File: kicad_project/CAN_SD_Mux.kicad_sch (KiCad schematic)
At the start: 2 parts, among them U13 ADG733BRU

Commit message: ERC passing!
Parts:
- removed unit 5 of U13
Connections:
- net +3.3V: now also U13.1; no longer U13.2
- net CAN_BUS: now also U13.12; no longer U13.13
- net GPOUT2: now also U13.13; no longer U13.12
- net SPI.CAN_SD_CS: now also U13.2; no longer U13.1
- net ~SD_CARD_ENABLE renamed SD_CARD_ENABLE

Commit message: Cleanups and more documentation
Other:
- moved on the sheet: C32, U13D
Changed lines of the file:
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@@
 	(generator "eeschema")
 	(generator_version "8.0")
-	(paper "A4")
+	(paper "A5")
+	(title_block
+		(comment 1 "Mux for selecting CAN signals.")
+	)
 	(junction
-		(at 57.15 172.72)
+		(at 137.16 86.36)
 		(diameter 0)
 		(color 0 0 0 0)
@@
 	)
 	(junction
-		(at 38.1 143.51)
+		(at 118.11 57.15)
 		(diameter 0)
 		(color 0 0 0 0)
 	)
 	(junction
-		(at 38.1 172.72)
+		(at 118.11 86.36)
 		(diameter 0)
 		(color 0 0 0 0)
@@
 	)
 	(junction
-		(at 44.45 172.72)
+		(at 124.46 86.36)
 		(diameter 0)
 		(color 0 0 0 0)
@@
 	(wire
 		(pts
-			(xy 35.56 142.24) (xy 35.56 143.51)
+			(xy 115.57 55.88) (xy 115.57 57.15)
 		)
 		(stroke
@@
 	(wire
 		(pts
-			(xy 38.1 143.51) (xy 57.15 143.51)
+			(xy 118.11 57.15) (xy 137.16 57.15)
 		)
 		(stroke
@@
 	(wire
 		(pts
-			(xy 44.45 172.72) (xy 38.1 172.72)
+			(xy 124.46 86.36) (xy 118.11 86.36)
 		)
 		(stroke
@@
 	(wire
 		(pts
-			(xy 44.45 158.75) (xy 44.45 172.72)
+			(xy 124.46 72.39) (xy 124.46 86.36)
 		)
 		(stroke
@@
 	(wire
 		(pts
-			(xy 35.56 143.51) (xy 38.1 143.51)
+			(xy 115.57 57.15) (xy 118.11 57.15)
 		)
 		(stroke
@@
 	(wire
 		(pts
-			(xy 57.15 143.51) (xy 57.15 146.05)
+			(xy 137.16 57.15) (xy 137.16 59.69)
 		)
 		(stroke
@@
 	(wire
 		(pts
-			(xy 49.53 158.75) (xy 44.45 158.75)
+			(xy 129.54 72.39) (xy 124.46 72.39)
 		)
 		(stroke
@@
 	(wire
 		(pts
-			(xy 38.1 172.72) (xy 35.56 172.72)
-		)
-		(stroke
-			(width 0)
-			(type default)
-		)
-	)
-	(wire
-		(pts
-			(xy 59.69 171.45) (xy 59.69 172.72)
+			(xy 118.11 86.36) (xy 115.57 86.36)
+		)
+		(stroke
+			(width 0)
+			(type default)
+		)
+	)
+	(wire
+		(pts
+			(xy 139.7 85.09) (xy 139.7 86.36)
 		)
 		(stroke
@@
 	(wire
 		(pts
-			(xy 38.1 153.67) (xy 38.1 172.72)
-		)
-		(stroke
-			(width 0)
-			(type default)
-		)
-	)
-	(wire
-		(pts
-			(xy 35.56 172.72) (xy 35.56 173.99)
+			(xy 118.11 67.31) (xy 118.11 86.36)
+		)
+		(stroke
+			(width 0)
+			(type default)
+		)
+	)
+	(wire
+		(pts
+			(xy 115.57 86.36) (xy 115.57 87.63)
 		)
 		(stroke
@@
 	(wire
 		(pts
-			(xy 59.69 172.72) (xy 57.15 172.72)
+			(xy 139.7 86.36) (xy 137.16 86.36)
 		)
 		(stroke
@@
 	(wire
 		(pts
-			(xy 57.15 172.72) (xy 44.45 172.72)
-		)
-		(stroke
-			(width 0)
-			(type default)
-		)
-	)
-	(wire
-		(pts
-			(xy 38.1 143.51) (xy 38.1 148.59)
+			(xy 137.16 86.36) (xy 124.46 86.36)
+		)
+		(stroke
+			(width 0)
+			(type default)
+		)
+	)
+	(wire
+		(pts
+			(xy 118.11 57.15) (xy 118.11 62.23)
 		)
 		(stroke
@@
 	(wire
 		(pts
-			(xy 57.15 171.45) (xy 57.15 172.72)
+			(xy 137.16 85.09) (xy 137.16 86.36)
 		)
 		(stroke
@@
 	(symbol
 		(lib_id "power:GND")
-		(at 35.56 173.99 0)
+		(at 115.57 87.63 0)
 		(unit 1)
 		(exclude_from_sim no)
@@
 		(fields_autoplaced yes)
 		(property "Reference" "#PWR0105"
-			(at 35.56 180.34 0)
+			(at 115.57 93.98 0)
 			(effects
 				(font
@@
 		)
 		(property "Value" "GND"
-			(at 35.56 179.07 0)
+			(at 115.57 92.71 0)
 			(effects
 				(font
@@
 		)
 		(property "Footprint" ""
-			(at 35.56 173.99 0)
+			(at 115.57 87.63 0)
 			(effects
 				(font
@@
 		)
 		(property "Datasheet" ""
-			(at 35.56 173.99 0)
+			(at 115.57 87.63 0)
 			(effects
 				(font
@@
 		)
 		(property "Description" "Power symbol creates a global label with name \"GND\" , ground"
-			(at 35.56 173.99 0)
+			(at 115.57 87.63 0)
 			(effects
 				(font
@@
 	(symbol
 		(lib_id "Device:C_Small")
-		(at 38.1 151.13 180)
+		(at 118.11 64.77 180)
 		(unit 1)
 		(exclude_from_sim no)
@@
 		(fields_autoplaced yes)
 		(property "Reference" "C32"
-			(at 40.64 149.8536 0)
+			(at 120.65 63.4936 0)
 			(effects
 				(font
@@
 		)
 		(property "Value" "100nF"
-			(at 40.64 152.3936 0)
+			(at 120.65 66.0336 0)
 			(effects
 				(font
@@
 		)
 		(property "Footprint" "Capacitor_SMD:C_1206_3216Metric"
-			(at 38.1 151.13 0)
+			(at 118.11 64.77 0)
 			(effects
 				(font
@@
 		)
 		(property "Datasheet" "~"
-			(at 38.1 151.13 0)
+			(at 118.11 64.77 0)
 			(effects
 				(font
@@
 		)
 		(property "Description" "Unpolarized capacitor, small symbol"
-			(at 38.1 151.13 0)
+			(at 118.11 64.77 0)
 			(effects
 				(font
@@
 		)
 		(property "SKU" ""
-			(at 38.1 151.13 0)
+			(at 118.11 64.77 0)
 			(effects
 				(font
@@
 		)
 		(property "Supplier" "Digi-Key"
-			(at 38.1 151.13 0)
+			(at 118.11 64.77 0)
 			(effects
 				(font
@@
 		)
 		(property "LibRef" "GRM319R72A104KA01D"
-			(at 38.1 151.13 0)
+			(at 118.11 64.77 0)
 			(effects
 				(font
@@
 	)
 	(symbol
-		(lib_name "ADG733BRU_2")
 		(lib_id "Analog_Switch:ADG733BRU")
 		(at 72.39 111.76 0)
@@
 	)
 	(symbol
-		(lib_name "ADG733BRU_4")
 		(lib_id "Analog_Switch:ADG733BRU")
 		(at 73.66 55.88 0)
@@
 	(symbol
 		(lib_id "power:+3.3V")
-		(at 35.56 142.24 0)
+		(at 115.57 55.88 0)
 		(unit 1)
 		(exclude_from_sim no)
@@
 		(fields_autoplaced yes)
 		(property "Reference" "#PWR051"
-			(at 35.56 146.05 0)
+			(at 115.57 59.69 0)
 			(effects
 				(font
@@
 		)
 		(property "Value" "+3.3V"
-			(at 35.56 137.16 0)
+			(at 115.57 50.8 0)
 			(effects
 				(font
@@
 		)
 		(property "Footprint" ""
-			(at 35.56 142.24 0)
+			(at 115.57 55.88 0)
 			(effects
 				(font
@@
 		)
 		(property "Datasheet" ""
-			(at 35.56 142.24 0)
+			(at 115.57 55.88 0)
 			(effects
 				(font
@@
 		)
 		(property "Description" "Power symbol creates a global label with name \"+3.3V\""
-			(at 35.56 142.24 0)
+			(at 115.57 55.88 0)
 			(effects
 				(font
@@
 	)
 	(symbol
-		(lib_name "ADG733BRU_3")
 		(lib_id "Analog_Switch:ADG733BRU")
-		(at 57.15 158.75 0)
+		(at 137.16 72.39 0)
 		(unit 4)
 		(exclude_from_sim no)
@@
 		(fields_autoplaced yes)
 		(property "Reference" "U13"
-			(at 66.04 157.48 0)
+			(at 146.05 71.12 0)
 			(effects
 				(font
@@
 		)
 		(property "Value" "ADG733BRU"
-			(at 66.04 160.02 0)
+			(at 146.05 73.66 0)
 			(effects
 				(font
@@
 		)
 		(property "Footprint" "Package_SO:TSSOP-16_4.4x5mm_P0.65mm"
-			(at 57.15 158.75 0)
+			(at 137.16 72.39 0)
 			(effects
 				(font
@@
 		)
 		(property "Datasheet" "https://www.analog.com/media/en/technical-documentation/data-sheets/ADG733_734.pdf"
-			(at 57.15 158.75 0)
+			(at 137.16 72.39 0)
 			(effects
 				(font
@@
 		)
 		(property "Description" "Triple SPDT CMOS Analog Switch, 2.5Ohm Ron, TSSOP-16"
-			(at 57.15 158.75 0)
+			(at 137.16 72.39 0)
 			(effects
 				(font
@@
 		)
 		(property "SKU" "ADG733BRUZ-REEL7CT-ND"
-			(at 57.15 158.75 0)
+			(at 137.16 72.39 0)
 			(effects
 				(font
@@
 		)
 		(property "Supplier" "Digi-Key"
-			(at 57.15 158.75 0)
+			(at 137.16 72.39 0)
 			(effects
 				(font
@@
 	)
 	(symbol
-		(lib_name "ADG733BRU_1")
 		(lib_id "Analog_Switch:ADG733BRU")
 		(at 73.66 85.09 0)

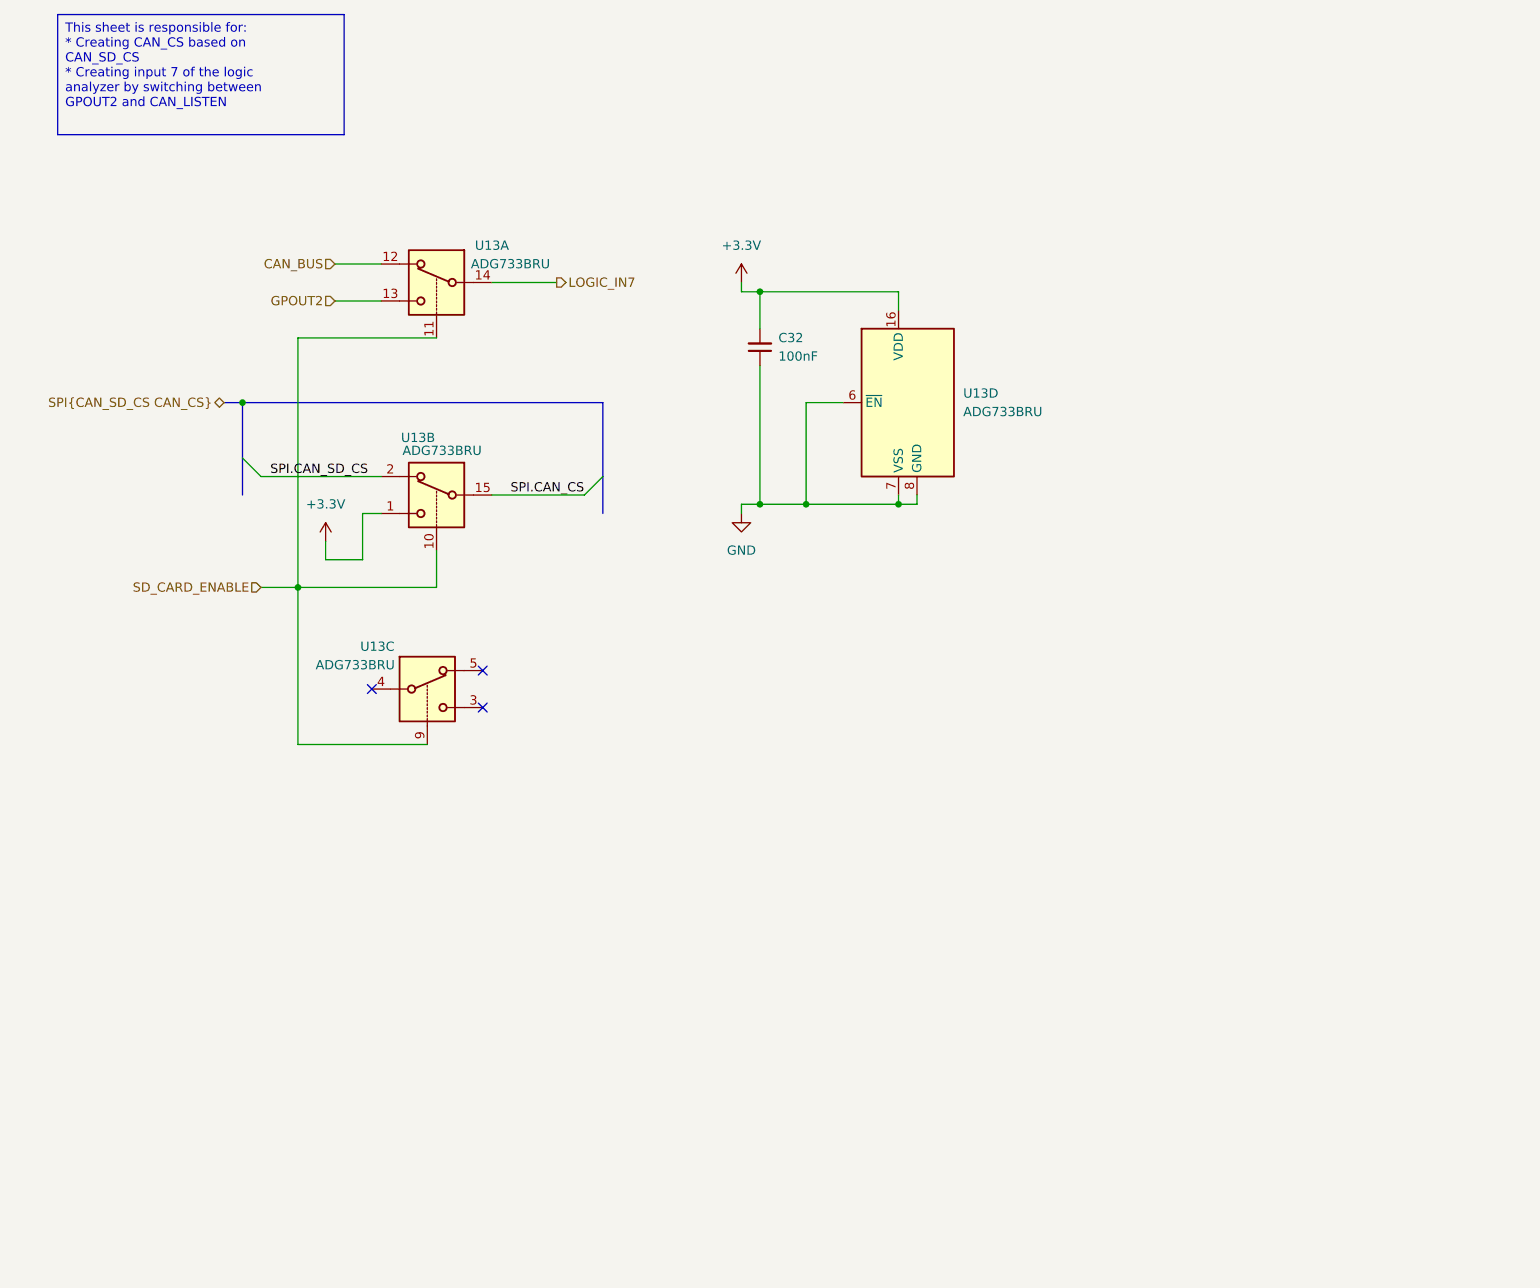
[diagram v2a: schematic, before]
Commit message: Finish new SD card schematic, ERC passing!
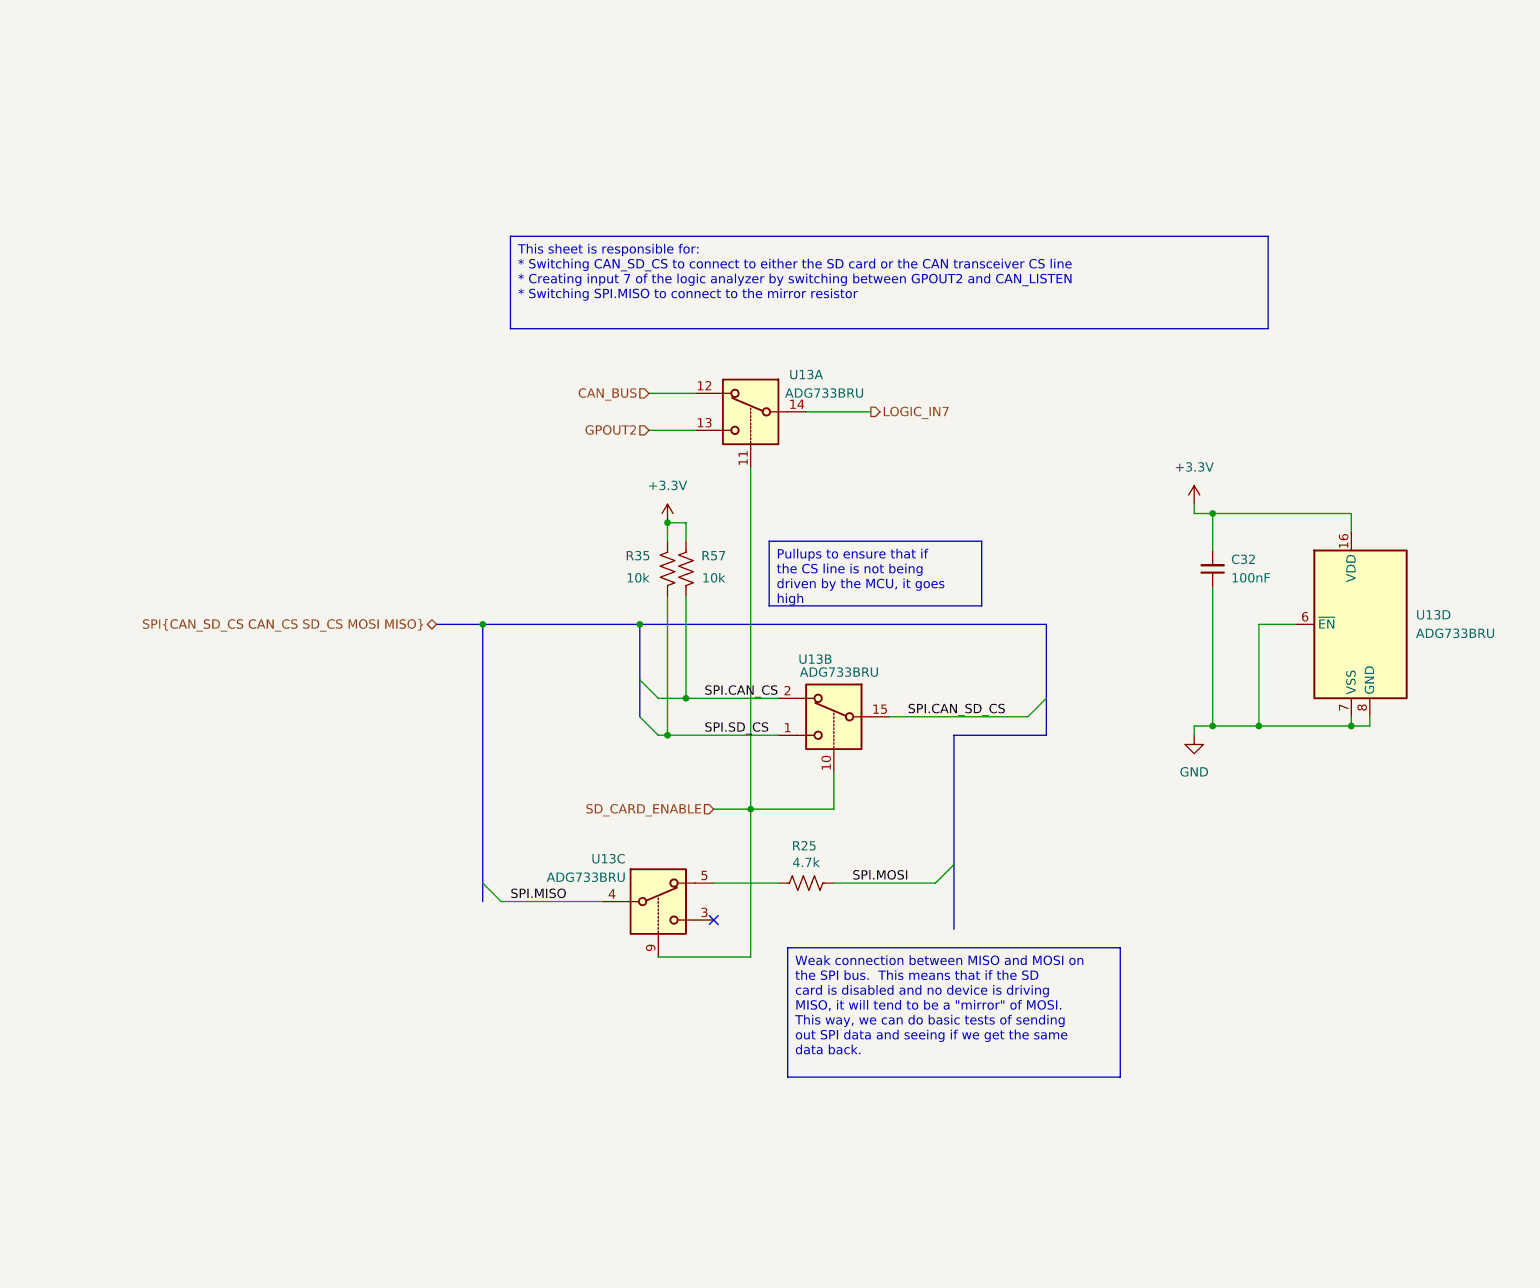
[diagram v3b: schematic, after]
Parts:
- added R25: 4.7k, Resistor_SMD:R_1206_3216Metric, symbol Device:R_US
- added R35, R57: 10k, Resistor_SMD:R_1206_3216Metric, symbol Device:R_US
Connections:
- net +3.3V: now also R35.2, R57.2; no longer U13.1
- net SPI.CAN_CS: now also U13.2, R57.1; no longer U13.15
- net SPI.CAN_SD_CS: now also U13.15; no longer U13.2
- net SPI.MISO: now reaches U13.4
- net at U13.5: now also R25.1
- new net SPI.MOSI: R25.2
- new net SPI.SD_CS: R35.1, U13.1
- no-connect marks 3 -> 1
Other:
- moved on the sheet: C32, U13A, U13B, U13C, U13D

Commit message: Oops, fix wrong LibRef for 4.7k resistor
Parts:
- R25: LibRef ERJ-8ENF4702V -> ERJ-8ENF4701V
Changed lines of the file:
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@@
 			)
 		)
-		(property "LibRef" "ERJ-8ENF4702V"
+		(property "LibRef" "ERJ-8ENF4701V"
 			(at 124.46 138.43 0)
 			(effects
